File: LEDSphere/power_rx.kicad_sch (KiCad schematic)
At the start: 11 parts, among them U101 DRV5032FCDBZR

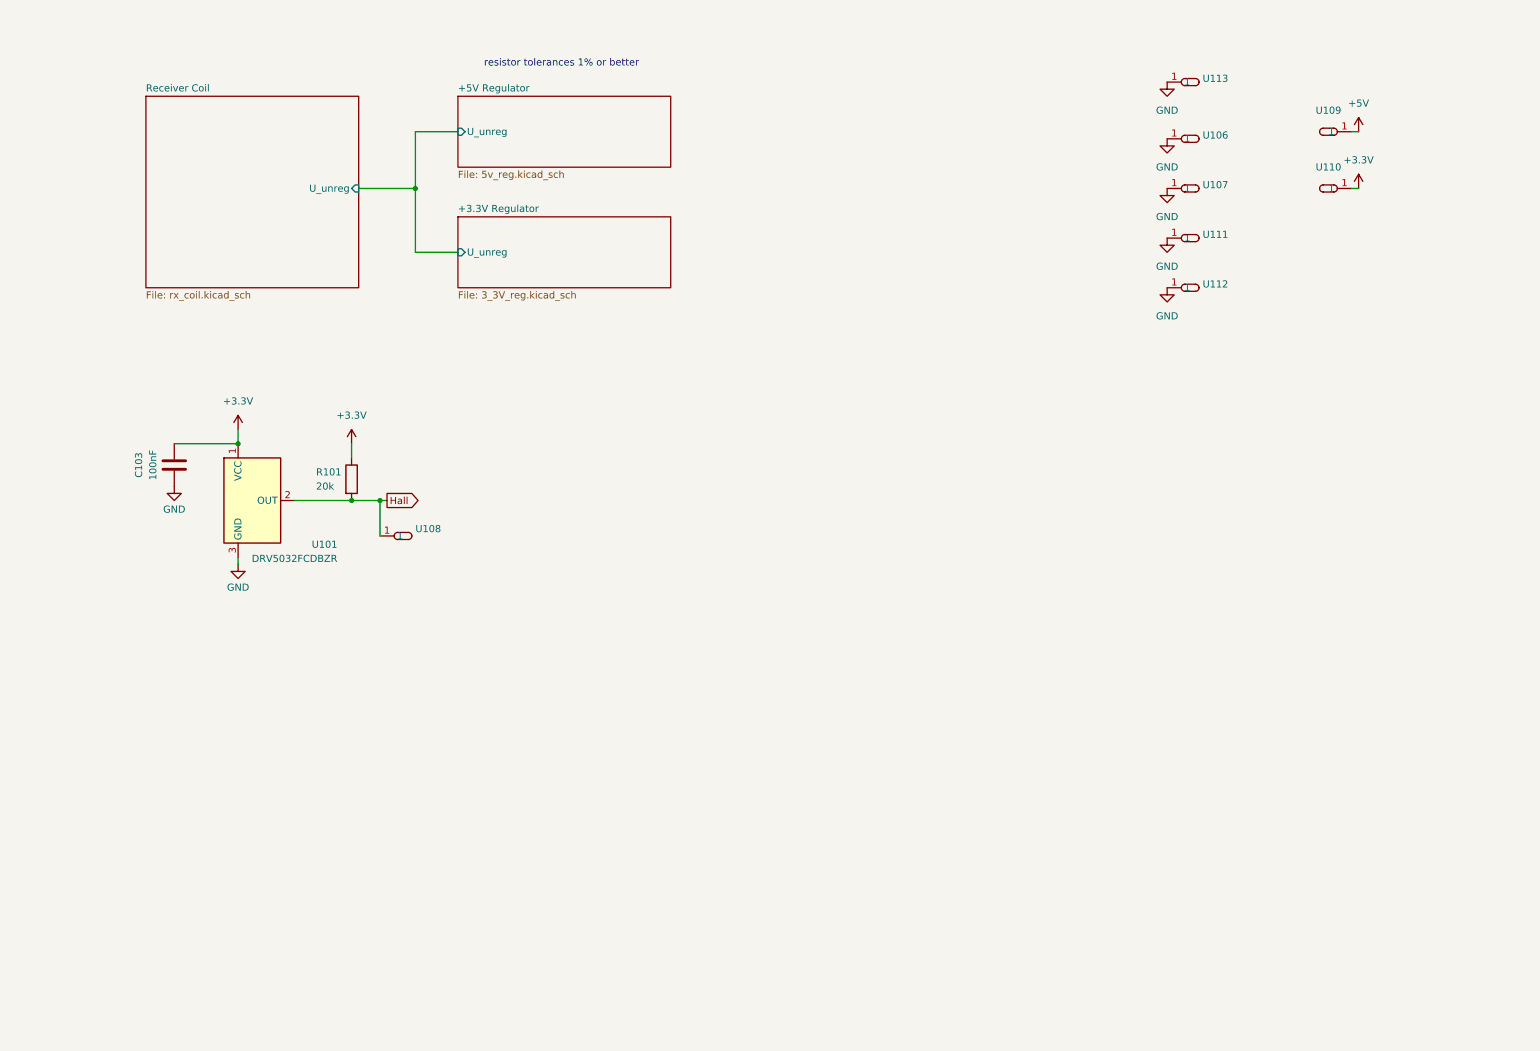
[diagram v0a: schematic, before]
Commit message: Modify RX Schm. + Adjusted TX Coil
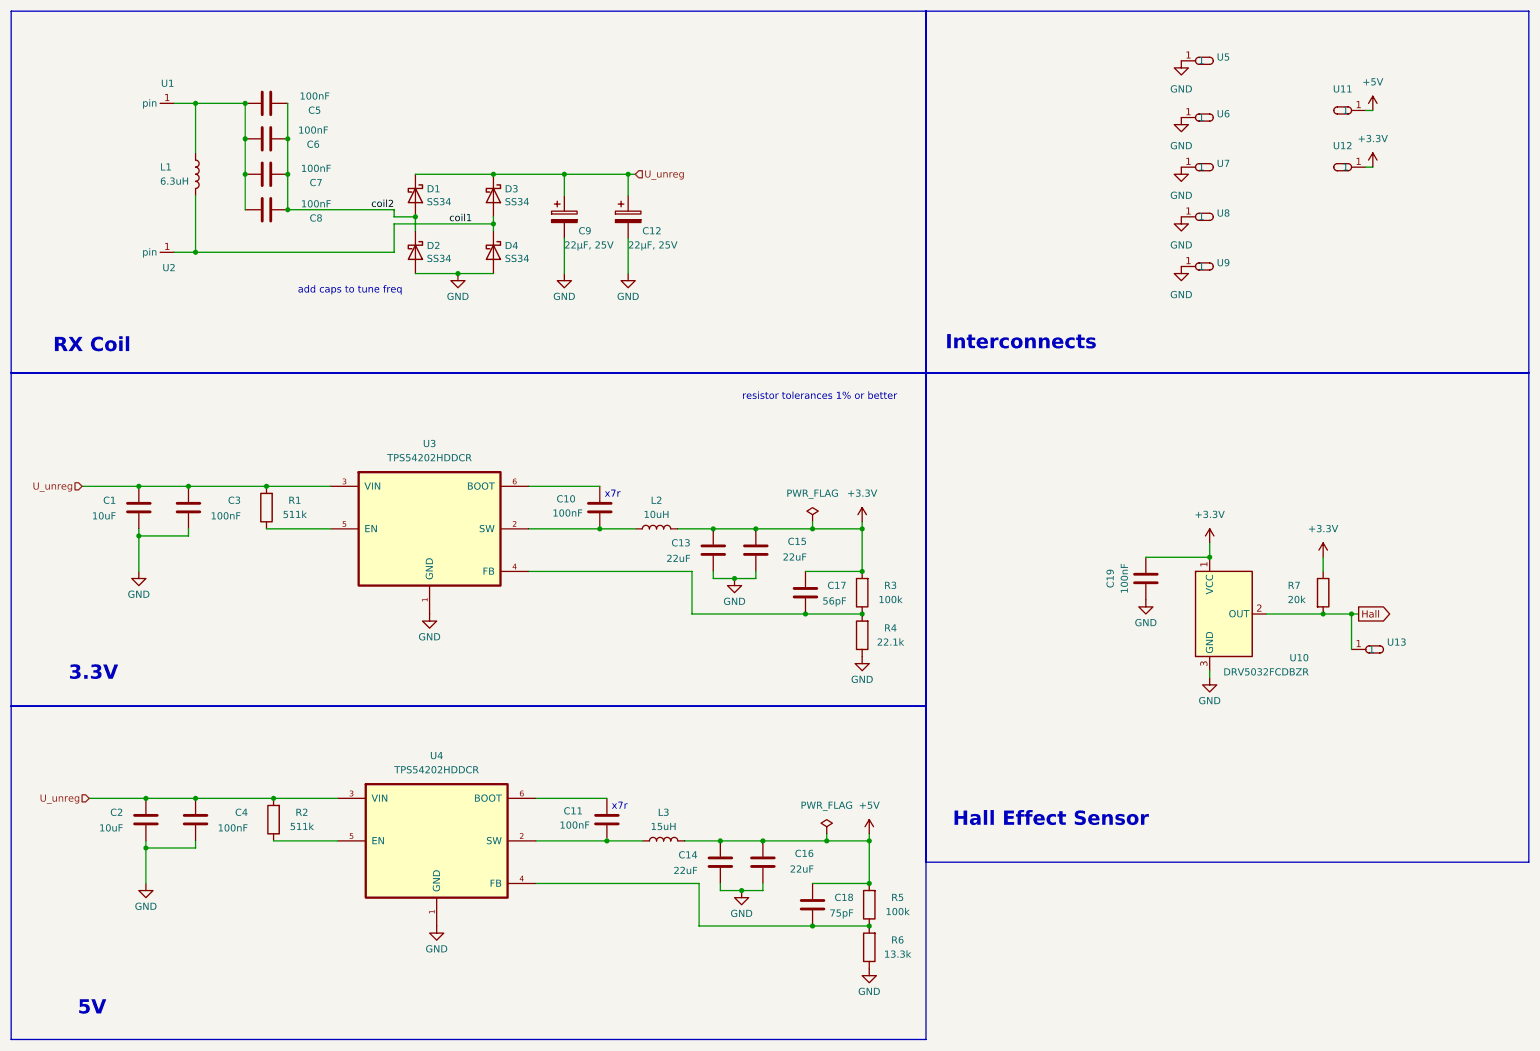
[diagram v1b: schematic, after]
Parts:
- added C1, C2: 10uF, Capacitor_SMD:C_0402_1005Metric, symbol Device:C
- added C10, C11, C3, C4, C5, C6, C7, C8: 100nF, Capacitor_SMD:C_0402_1005Metric, symbol Device:C
- added C12, C9: 22µF, 25V, Capacitor_SMD:C_0805_2012Metric, symbol RD40_display_SMD-rescue:CP-Device
- added C13, C14, C15, C16: 22uF, Capacitor_SMD:C_0402_1005Metric, symbol Device:C
- added C17: 56pF, Capacitor_SMD:C_0402_1005Metric, symbol Device:C
- added C18: 75pF, Capacitor_SMD:C_0402_1005Metric, symbol Device:C
- added D1, D2, D3, D4: SS34, Diode_SMD:D_SMA, symbol Device:D_Schottky
- added L1: 6.3uH, symbol Device:L
- added L2: 10uH, Inductor_SMD:L_Abracon_ASPI-0630LR, symbol Device:L
- added L3: 15uH, Inductor_SMD:L_Abracon_ASPI-0630LR, symbol Device:L
- added R1, R2: 511k, Resistor_SMD:R_0402_1005Metric, symbol Device:R
- added R3, R5: 100k, Resistor_SMD:R_0402_1005Metric, symbol Device:R
- added R4: 22.1k, Resistor_SMD:R_0402_1005Metric, symbol Device:R
- added R6: 13.3k, Resistor_SMD:R_0402_1005Metric, symbol Device:R
- added U1, U2: (no value), my_footprints:Pin_D1.0mm, symbol my_symbols:pin
- added U3, U4: TPS54202HDDCR, Footprints:SOT95P280X110-6N, symbol TPS54202HDDCR:TPS54202HDDCR
- U11: renamed from U109; value ~ -> (none)
- U12: renamed from U110; value ~ -> (none)
- U13: renamed from U108; value ~ -> (none)
- U5: renamed from U113; value ~ -> (none)
- U6: renamed from U106; value ~ -> (none)
- U7: renamed from U107; value ~ -> (none)
- U8: renamed from U111; value ~ -> (none)
- U9: renamed from U112; value ~ -> (none)
- renumbered C103 to C19, R101 to R7, U101 to U10
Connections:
- net +3.3V: now also C13.2, C15.2, C17.2, L2.2, R3.2
- net +5V: now also C14.2, C16.2, C18.2, L3.2, R5.2
- net GND: now also C1.1, C12.2, C13.1, C14.1, C15.1, C16.1, C2.1, C3.1, C4.1, C9.2, D2.2 (A), D4.2 (A), R4.1, R6.1, U3.1 (GND), U4.1 (GND)
- new net: C17.1, R3.1, R4.2, U3.4 (FB)
- new net: C18.1, R5.1, R6.2, U4.4 (FB)
- new net: C5.1, C6.1, C7.1, C8.1, L1.1, U1.1 (pin)
- new net: R1.1, U3.5 (EN)
- new net: C11.1, L3.1, U4.2 (SW)
- new net: C11.2, U4.6 (BOOT)
- new net: C10.1, L2.1, U3.2 (SW)
- new net: R2.1, U4.5 (EN)
- new net: C10.2, U3.6 (BOOT)
- new net U_unreg: C1.2, C12.1, C2.2, C3.2, C4.2, C9.1, D1.1 (K), D3.1 (K), R1.2, R2.2, U3.3 (VIN), U4.3 (VIN)
- new net coil1: D3.2 (A), D4.1 (K), L1.2, U2.1 (pin)
- new net coil2: C5.2, C6.2, C7.2, C8.2, D1.2 (A), D2.1 (K)
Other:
- removed sheet +3.3V Regulator
- removed sheet +5V Regulator
- removed sheet Receiver Coil
- note added: "3.3V"
- note added: "5V"
- note added: "Hall Effect Sensor"
- note added: "Interconnects"
- note added: "RX Coil"
- note added: "add caps to tune freq"
- note added: "x7r"
- moved on the sheet: C19, R7, U10, U11, U12, U13, U5, U6, U7, U8, U9

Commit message: first draft rx power layout
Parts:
- C1, C13, C14, C15, C16, C2: footprint Capacitor_SMD:C_0402_1005Metric -> Capacitor_SMD:C_1206_3216Metric
- C12, C9: footprint Capacitor_SMD:C_0805_2012Metric -> Capacitor_SMD:C_1206_3216Metric
- L1: value 6.3uH -> 5.86uH
- R3, R4, R5, R6, R7: footprint Resistor_SMD:R_0402_1005Metric -> Resistor_SMD:R_0603_1608Metric
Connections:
- net coil2: now also C5.1, C6.1, C7.1, C8.1, L1.1, U1.1 (pin); no longer C5.2, C6.2, C7.2, C8.2, D1.2 (A), D2.1 (K)
- new net: C5.2, C6.2, C7.2, C8.2, D1.2 (A), D2.1 (K)
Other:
- moved on the sheet: U1, U2

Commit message: change footprints
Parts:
- C12, C13, C14, C15, C16, C9: footprint Capacitor_SMD:C_1206_3216Metric -> Capacitor_SMD:C_1210_3225Metric
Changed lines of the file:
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@@
 			)
 		)
-		(property "Footprint" "Capacitor_SMD:C_1206_3216Metric"
+		(property "Footprint" "Capacitor_SMD:C_1210_3225Metric"
 			(at 145.0848 106.68 0)
 			(hide yes)
@@
 			)
 		)
-		(property "Footprint" "Capacitor_SMD:C_1206_3216Metric"
+		(property "Footprint" "Capacitor_SMD:C_1210_3225Metric"
 			(at 112.7252 54.61 0)
 			(hide yes)
@@
 			)
 		)
-		(property "Footprint" "Capacitor_SMD:C_1206_3216Metric"
+		(property "Footprint" "Capacitor_SMD:C_1210_3225Metric"
 			(at 138.7348 162.56 0)
 			(hide yes)
@@
 			)
 		)
-		(property "Footprint" "Capacitor_SMD:C_1206_3216Metric"
+		(property "Footprint" "Capacitor_SMD:C_1210_3225Metric"
 			(at 146.3548 162.56 0)
 			(hide yes)
@@
 			)
 		)
-		(property "Footprint" "Capacitor_SMD:C_1206_3216Metric"
+		(property "Footprint" "Capacitor_SMD:C_1210_3225Metric"
 			(at 137.4648 106.68 0)
 			(hide yes)
@@
 			)
 		)
-		(property "Footprint" "Capacitor_SMD:C_1206_3216Metric"
+		(property "Footprint" "Capacitor_SMD:C_1210_3225Metric"
 			(at 124.1552 54.61 0)
 			(hide yes)

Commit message: power rx layout change
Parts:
- removed C12, C9: 22µF, 25V, Capacitor_SMD:C_1210_3225Metric, symbol RD40_display_SMD-rescue:CP-Device
- added C12, C9: 22uF, Capacitor_SMD:C_1210_3225Metric, symbol Device:C
- C5, C6, C7, C8: footprint Capacitor_SMD:C_0402_1005Metric -> Capacitor_SMD:C_0603_1608Metric
- L2, L3: footprint Inductor_SMD:L_Abracon_ASPI-0630LR -> Inductor_SMD:L_Vishay_IHLP-3232
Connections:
- net GND: now also C12.1, C9.1
- net U_unreg: now also C12.2, C9.2
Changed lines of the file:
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@@
 	)
 	(symbol
-		(lib_id "RD40_display_SMD-rescue:CP-Device")
-		(at 111.76 50.8 0)
-		(unit 1)
-		(body_style 1)
-		(exclude_from_sim no)
-		(in_bom yes)
-		(on_board yes)
-		(in_pos_files yes)
-		(dnp no)
-		(property "Reference" "C9"
-			(at 114.3 53.34 0)
-			(show_name no)
-			(do_not_autoplace no)
-			(effects
-				(font
-					(size 1.27 1.27)
-				)
-				(justify left)
-			)
-		)
-		(property "Value" "22µF, 25V"
-			(at 111.76 55.88 0)
-			(show_name no)
-			(do_not_autoplace no)
-			(effects
-				(font
-					(size 1.27 1.27)
-				)
-				(justify left)
-			)
-		)
-		(property "Footprint" "Capacitor_SMD:C_1210_3225Metric"
-			(at 112.7252 54.61 0)
-			(hide yes)
-			(show_name no)
-			(do_not_autoplace no)
-			(effects
-				(font
-					(size 1.27 1.27)
-				)
-			)
-		)
-		(property "Datasheet" ""
-			(at 111.76 50.8 0)
-			(hide yes)
-			(show_name no)
-			(do_not_autoplace no)
-			(effects
-				(font
-					(size 1.27 1.27)
-				)
-			)
-		)
-		(property "Description" ""
-			(at 111.76 50.8 0)
-			(hide yes)
-			(show_name no)
-			(do_not_autoplace no)
-			(effects
-				(font
-					(size 1.27 1.27)
-				)
-			)
-		)
-		(property "LCSC" "C45783"
-			(at 111.76 50.8 0)
-			(hide yes)
-			(show_name no)
-			(do_not_autoplace no)
-			(effects
-				(font
-					(size 1.27 1.27)
-				)
-			)
-		)
-		(pin "1"
-		)
-		(pin "2"
-		)
-		(instances
-			(project "power_rx"
-				(path "/ddd18393-06be-4266-b885-a3f36c5c5ced"
-					(reference "C9")
-					(unit 1)
-				)
-			)
-		)
-	)
-	(symbol
 		(lib_id "Device:R")
 		(at 58.42 102.87 180)
@@
 			)
 		)
-		(property "Footprint" "Capacitor_SMD:C_0402_1005Metric"
+		(property "Footprint" "Capacitor_SMD:C_0603_1608Metric"
 			(at 62.23 42.2148 0)
 			(hide yes)
@@
 			)
 		)
-		(property "Footprint" "Capacitor_SMD:C_0402_1005Metric"
+		(property "Footprint" "Capacitor_SMD:C_0603_1608Metric"
 			(at 62.23 35.8648 0)
 			(hide yes)
@@
 			)
 		)
-		(property "Footprint" "Inductor_SMD:L_Abracon_ASPI-0630LR"
+		(property "Footprint" "Inductor_SMD:L_Vishay_IHLP-3232"
 			(at 129.54 162.56 0)
 			(hide yes)
@@
 			)
 		)
-		(property "Footprint" "Inductor_SMD:L_Abracon_ASPI-0630LR"
+		(property "Footprint" "Inductor_SMD:L_Vishay_IHLP-3232"
 			(at 128.27 106.68 0)
 			(hide yes)
@@
 	)
 	(symbol
+		(lib_id "Device:C")
+		(at 123.19 50.8 180)
+		(unit 1)
+		(body_style 1)
+		(exclude_from_sim no)
+		(in_bom yes)
+		(on_board yes)
+		(in_pos_files yes)
+		(dnp no)
+		(property "Reference" "C12"
+			(at 119.126 49.53 0)
+			(show_name no)
+			(do_not_autoplace no)
+			(effects
+				(font
+					(size 1.27 1.27)
+				)
+				(justify left)
+			)
+		)
+		(property "Value" "22uF"
+			(at 119.126 52.324 0)
+			(show_name no)
+			(do_not_autoplace no)
+			(effects
+				(font
+					(size 1.27 1.27)
+				)
+				(justify left)
+			)
+		)
+		(property "Footprint" "Capacitor_SMD:C_1210_3225Metric"
+			(at 122.2248 46.99 0)
+			(hide yes)
+			(show_name no)
+			(do_not_autoplace no)
+			(effects
+				(font
+					(size 1.27 1.27)
+				)
+			)
+		)
+		(property "Datasheet" ""
+			(at 123.19 50.8 0)
+			(hide yes)
+			(show_name no)
+			(do_not_autoplace no)
+			(effects
+				(font
+					(size 1.27 1.27)
+				)
+			)
+		)
+		(property "Description" ""
+			(at 123.19 50.8 0)
+			(hide yes)
+			(show_name no)
+			(do_not_autoplace no)
+			(effects
+				(font
+					(size 1.27 1.27)
+				)
+			)
+		)
+		(property "LCSC" "C307331"
+			(at 123.19 50.8 90)
+			(hide yes)
+			(show_name no)
+			(do_not_autoplace no)
+			(effects
+				(font
+					(size 1.27 1.27)
+				)
+			)
+		)
+		(pin "1"
+		)
+		(pin "2"
+		)
+		(instances
+			(project "power_rx"
+				(path "/ddd18393-06be-4266-b885-a3f36c5c5ced"
+					(reference "C12")
+					(unit 1)
+				)
+			)
+		)
+	)
+	(symbol
+		(lib_id "Device:C")
+		(at 111.76 50.8 180)
+		(unit 1)
+		(body_style 1)
+		(exclude_from_sim no)
+		(in_bom yes)
+		(on_board yes)
+		(in_pos_files yes)
+		(dnp no)
+		(property "Reference" "C9"
+			(at 107.696 49.53 0)
+			(show_name no)
+			(do_not_autoplace no)
+			(effects
+				(font
+					(size 1.27 1.27)
+				)
+				(justify left)
+			)
+		)
+		(property "Value" "22uF"
+			(at 107.696 52.324 0)
+			(show_name no)
+			(do_not_autoplace no)
+			(effects
+				(font
+					(size 1.27 1.27)
+				)
+				(justify left)
+			)
+		)
+		(property "Footprint" "Capacitor_SMD:C_1210_3225Metric"
+			(at 110.7948 46.99 0)
+			(hide yes)
+			(show_name no)
+			(do_not_autoplace no)
+			(effects
+				(font
+					(size 1.27 1.27)
+				)
+			)
+		)
+		(property "Datasheet" ""
+			(at 111.76 50.8 0)
+			(hide yes)
+			(show_name no)
+			(do_not_autoplace no)
+			(effects
+				(font
+					(size 1.27 1.27)
+				)
+			)
+		)
+		(property "Description" ""
+			(at 111.76 50.8 0)
+			(hide yes)
+			(show_name no)
+			(do_not_autoplace no)
+			(effects
+				(font
+					(size 1.27 1.27)
+				)
+			)
+		)
+		(property "LCSC" "C307331"
+			(at 111.76 50.8 90)
+			(hide yes)
+			(show_name no)
+			(do_not_autoplace no)
+			(effects
+				(font
+					(size 1.27 1.27)
+				)
+			)
+		)
+		(pin "1"
+		)
+		(pin "2"
+		)
+		(instances
+			(project "power_rx"
+				(path "/ddd18393-06be-4266-b885-a3f36c5c5ced"
+					(reference "C9")
+					(unit 1)
+				)
+			)
+		)
+	)
+	(symbol
 		(lib_name "GND_1")
 		(lib_id "power:GND")
@@
 			)
 		)
-		(property "Footprint" "Capacitor_SMD:C_0402_1005Metric"
+		(property "Footprint" "Capacitor_SMD:C_0603_1608Metric"
 			(at 62.23 48.5648 0)
 			(hide yes)
@@
 			)
 		)
-		(property "Footprint" "Capacitor_SMD:C_0402_1005Metric"
+		(property "Footprint" "Capacitor_SMD:C_0603_1608Metric"
 			(at 62.23 29.5148 0)
 			(hide yes)
@@
 					(unit 1)
 				)
-			)
-		)
-	)
-	(symbol
-		(lib_id "RD40_display_SMD-rescue:CP-Device")
-		(at 123.19 50.8 0)
-		(unit 1)
-		(body_style 1)
-		(exclude_from_sim no)
-		(in_bom yes)
-		(on_board yes)
-		(in_pos_files yes)
-		(dnp no)
-		(property "Reference" "C12"
-			(at 125.73 53.34 0)
-			(show_name no)
-			(do_not_autoplace no)
-			(effects
-				(font
-					(size 1.27 1.27)
-				)
-				(justify left)
-			)
-		)
-		(property "Value" "22µF, 25V"
-			(at 123.19 55.88 0)
-			(show_name no)
-			(do_not_autoplace no)
-			(effects
-				(font
-					(size 1.27 1.27)
-				)
-				(justify left)
-			)
-		)
-		(property "Footprint" "Capacitor_SMD:C_1210_3225Metric"
-			(at 124.1552 54.61 0)
-			(hide yes)
-			(show_name no)
-			(do_not_autoplace no)
-			(effects
-				(font
-					(size 1.27 1.27)
-				)
-			)
-		)
-		(property "Datasheet" ""
-			(at 123.19 50.8 0)
-			(hide yes)
-			(show_name no)
-			(do_not_autoplace no)
-			(effects
-				(font
-					(size 1.27 1.27)
-				)
-			)
-		)
-		(property "Description" ""
-			(at 123.19 50.8 0)
-			(hide yes)
-			(show_name no)
-			(do_not_autoplace no)
-			(effects
-				(font
-					(size 1.27 1.27)
-				)
-			)
-		)
-		(property "LCSC" "C45783"
-			(at 123.19 50.8 0)
-			(hide yes)
-			(show_name no)
-			(do_not_autoplace no)
-			(effects
-				(font
-					(size 1.27 1.27)
-				)
-			)
-		)
-		(pin "1"
-		)
-		(pin "2"
-		)
-		(instances
-			(project "power_rx"
-				(path "/ddd18393-06be-4266-b885-a3f36c5c5ced"
-					(reference "C12")
-					(unit 1)
-				)
